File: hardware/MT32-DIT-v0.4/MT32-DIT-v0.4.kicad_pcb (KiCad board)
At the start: 2 copper layers, 105 x 53 mm, 31 parts, among them J1 DEMUX_IN, J2 PWR_IN, J3 I2S_CONN, SW1 PWR, U1 4050, U10 PCM54HP, U2 4050, U3 4050, U4 Gowin9K, U5 4050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

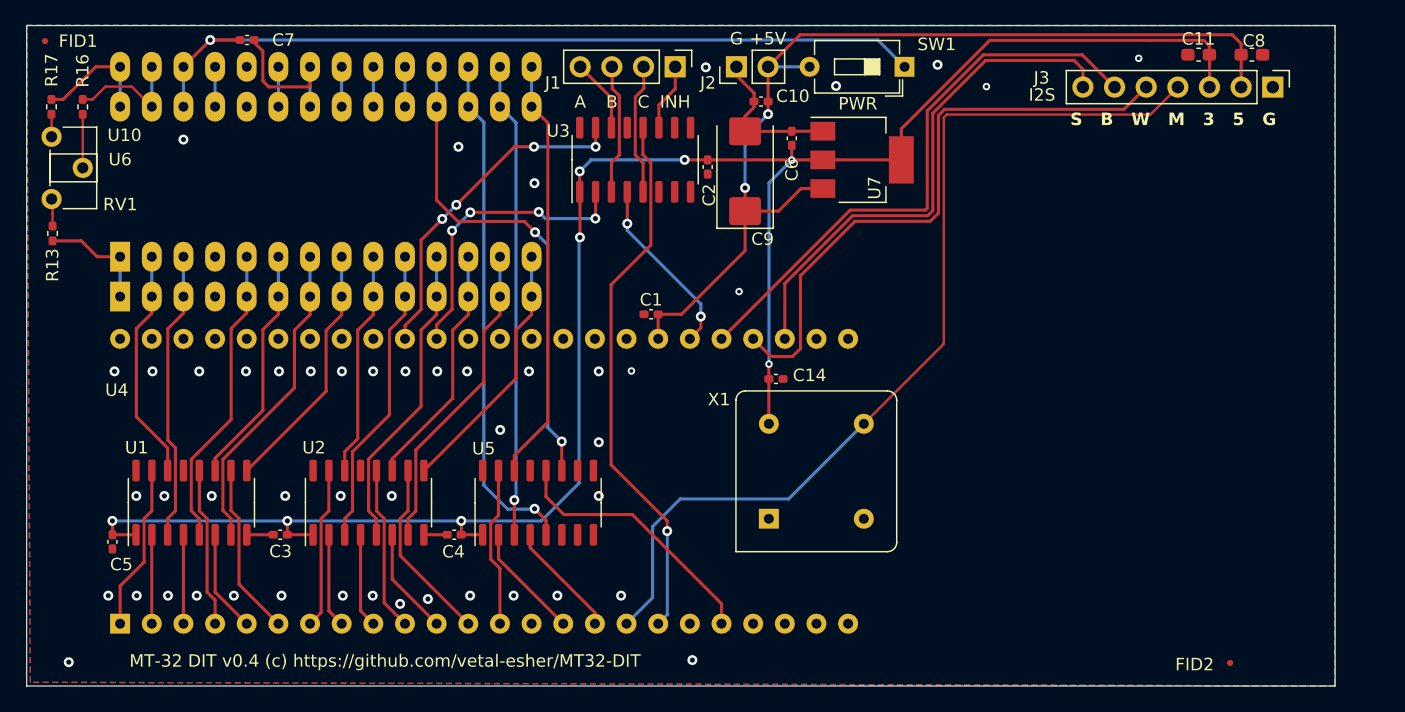
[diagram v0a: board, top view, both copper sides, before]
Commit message: Kicad 9.0.5 update
Kicad update to 9.0.5
Src change: dtr is back, second buffer register added
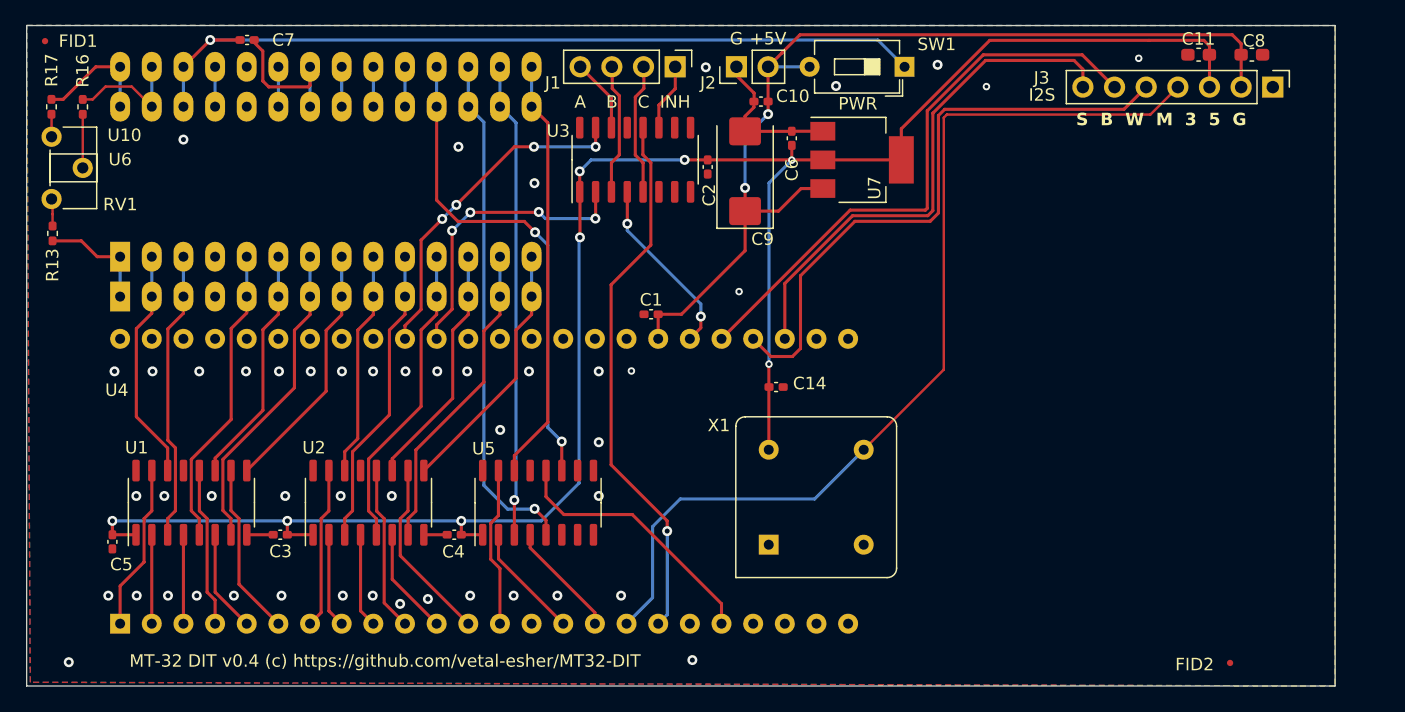
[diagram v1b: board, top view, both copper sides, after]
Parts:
- moved X1 2.08 mm to (205.3, 115.9)
- moved C14 0.65 mm to (205.9, 103.3)
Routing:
- net +3V3: track 155.7 -> 157.8 mm
- net MCLK: track 76.0 -> 77.3 mm

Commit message: HW updates
Service notes 2nd and 3rd editions added. Kicad schematic update - LSB bit route can be selected for external input.
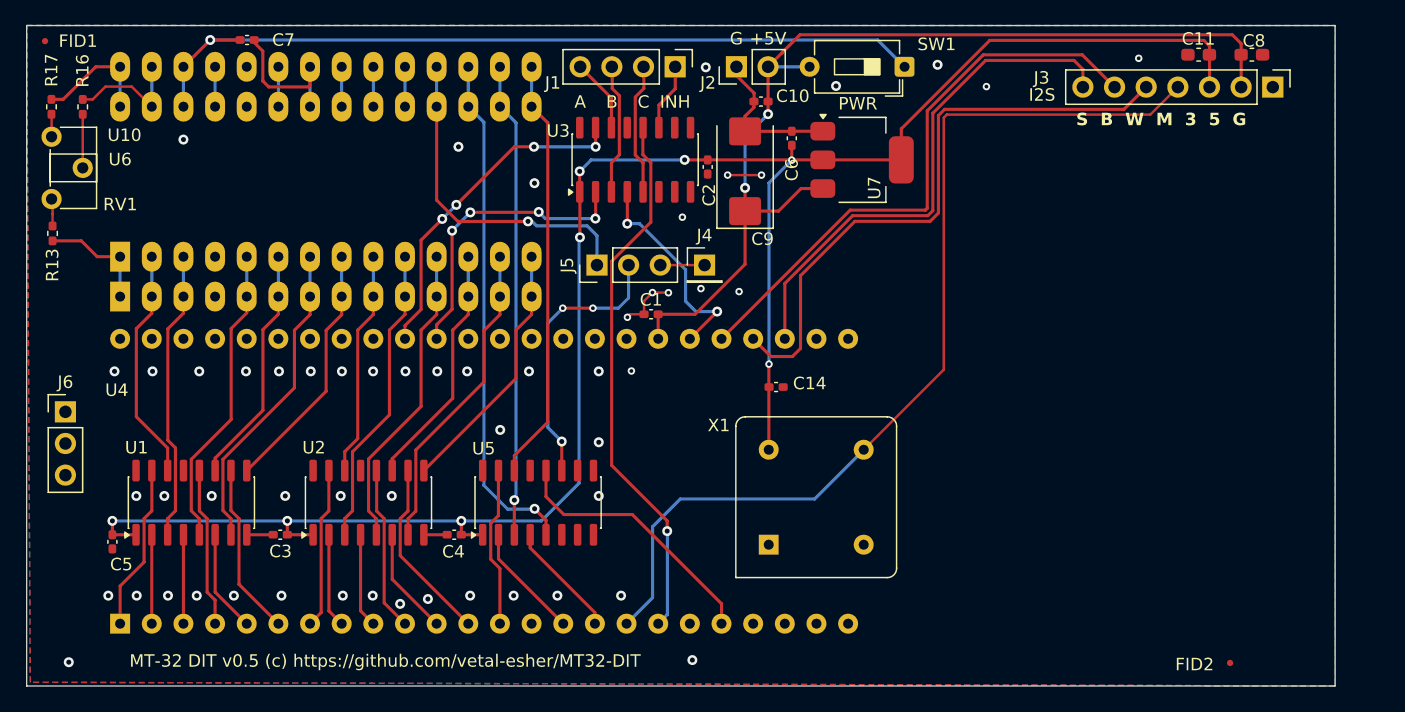
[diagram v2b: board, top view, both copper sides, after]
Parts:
- added J4: LSB, Connector_PinHeader_2.54mm:PinHeader_1x01_P2.54mm_Vertical, F.Cu at (200.2, 93.5)
- added J5: LSB_conn, Connector_PinHeader_2.54mm:PinHeader_1x03_P2.54mm_Vertical, F.Cu at (191.5, 93.5)
- added J6: GND hook, Connector_PinHeader_2.54mm:PinHeader_1x03_P2.54mm_Vertical, F.Cu at (148.9, 105.2)
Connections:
- U5 pad 11: P16 -> LSB
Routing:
- net LSB: track 0.00 -> 22.3 mm, vias 0 -> 3
- net P16: track 39.7 -> 27.1 mm, vias 2 -> 1
- net GNDREF: track 28.7 -> 36.1 mm, vias 48 -> 55
- net Net-(J4-Pin_1): track 0.00 -> 3.56 mm
- net CLK_C: track 14.6 -> 17.3 mm
- net +5V: track 79.7 -> 80.4 mm
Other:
- board text added: "MT-32 DIT v0.5 (c) https://github.com/vetal-esher/MT32-DIT"
- board text removed: "MT-32 DIT v0.4 (c) https://github.com/vetal-esher/MT32-DIT"
